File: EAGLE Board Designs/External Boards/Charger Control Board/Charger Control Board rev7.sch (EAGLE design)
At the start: 107 parts, among them K1 RELAY_DPDT, K2 RELAY_DPDT, K3 RELAY_DPDT, K4 RELAY_SOLIDSTATE_NO_, U1 VOLTAGE_REGULATOR_SOT-223_5V, U2 MCP2562FD, U3 LOGICGATE_BUFFER, U4 MCP2562FD, U7 ADM823

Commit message: Redid board layout/routing
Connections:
- net +12V: now also TP2.P$1
- net +3V3: now also TP11.P$1
- net +5V: now also TP1.P$1
- net BMS_OK: now also TP10.P$1
- net CCU_OK: now also TP8.P$1
- net GND: now also TP12.P$1
- net IMD_OK: now also TP9.P$1
- net SHDN_A: now also TP3.P$1
- net SHDN_B: now also TP4.P$1
- net SHDN_C: now also TP5.P$1
- net SHDN_D: now also TP6.P$1
- net SHDN_E: now also TP7.P$1
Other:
- moved on the sheet: TP1, TP10, TP11, TP12, TP2, TP3, TP4, TP5, TP6, TP7, TP8, TP9
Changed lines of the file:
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@@
 <attribute name="VALUE" x="134.62" y="54.61" size="1.27" layer="96" align="top-center"/>
 </instance>
-<instance part="TP6" gate="G$1" x="264.16" y="109.22" smashed="yes">
-<attribute name="NAME" x="261.62" y="110.998" size="1.27" layer="95"/>
-<attribute name="MPN" x="261.62" y="107.442" size="1.27" layer="95" align="top-left"/>
-</instance>
-<instance part="TP7" gate="G$1" x="264.16" y="101.6" smashed="yes">
-<attribute name="NAME" x="261.62" y="103.378" size="1.27" layer="95"/>
-<attribute name="MPN" x="261.62" y="99.822" size="1.27" layer="95" align="top-left"/>
-</instance>
-<instance part="TP8" gate="G$1" x="264.16" y="93.98" smashed="yes">
-<attribute name="NAME" x="261.62" y="95.758" size="1.27" layer="95"/>
-<attribute name="MPN" x="261.62" y="92.202" size="1.27" layer="95" align="top-left"/>
-</instance>
-<instance part="TP9" gate="G$1" x="264.16" y="86.36" smashed="yes">
-<attribute name="NAME" x="261.62" y="88.138" size="1.27" layer="95"/>
-<attribute name="MPN" x="261.62" y="84.582" size="1.27" layer="95" align="top-left"/>
-</instance>
-<instance part="TP10" gate="G$1" x="264.16" y="78.74" smashed="yes">
-<attribute name="NAME" x="261.62" y="80.518" size="1.27" layer="95"/>
-<attribute name="MPN" x="261.62" y="76.962" size="1.27" layer="95" align="top-left"/>
-</instance>
-<instance part="TP12" gate="G$1" x="264.16" y="71.12" smashed="yes">
-<attribute name="NAME" x="261.62" y="72.898" size="1.27" layer="95"/>
-<attribute name="MPN" x="261.62" y="69.342" size="1.27" layer="95" align="top-left"/>
-</instance>
-<instance part="TP1" gate="G$1" x="193.04" y="101.6" smashed="yes">
-<attribute name="NAME" x="190.5" y="103.378" size="1.27" layer="95"/>
-<attribute name="MPN" x="190.5" y="99.822" size="1.27" layer="95" align="top-left"/>
-</instance>
-<instance part="TP2" gate="G$1" x="193.04" y="93.98" smashed="yes">
-<attribute name="NAME" x="190.5" y="95.758" size="1.27" layer="95"/>
-<attribute name="MPN" x="190.5" y="92.202" size="1.27" layer="95" align="top-left"/>
-</instance>
-<instance part="TP3" gate="G$1" x="193.04" y="86.36" smashed="yes">
-<attribute name="NAME" x="190.5" y="88.138" size="1.27" layer="95"/>
-<attribute name="MPN" x="190.5" y="84.582" size="1.27" layer="95" align="top-left"/>
-</instance>
-<instance part="TP4" gate="G$1" x="193.04" y="78.74" smashed="yes">
-<attribute name="NAME" x="190.5" y="80.518" size="1.27" layer="95"/>
-<attribute name="MPN" x="190.5" y="76.962" size="1.27" layer="95" align="top-left"/>
-</instance>
-<instance part="TP5" gate="G$1" x="193.04" y="71.12" smashed="yes">
-<attribute name="NAME" x="190.5" y="72.898" size="1.27" layer="95"/>
-<attribute name="MPN" x="190.5" y="69.342" size="1.27" layer="95" align="top-left"/>
-</instance>
-<instance part="TP11" gate="G$1" x="193.04" y="109.22" smashed="yes">
-<attribute name="NAME" x="190.5" y="110.998" size="1.27" layer="95"/>
-<attribute name="MPN" x="190.5" y="107.442" size="1.27" layer="95" align="top-left"/>
+<instance part="TP6" gate="G$1" x="223.52" y="109.22" smashed="yes">
+<attribute name="NAME" x="220.98" y="110.998" size="1.27" layer="95"/>
+<attribute name="MPN" x="220.98" y="107.442" size="1.27" layer="95" align="top-left"/>
+</instance>
+<instance part="TP7" gate="G$1" x="223.52" y="101.6" smashed="yes">
+<attribute name="NAME" x="220.98" y="103.378" size="1.27" layer="95"/>
+<attribute name="MPN" x="220.98" y="99.822" size="1.27" layer="95" align="top-left"/>
+</instance>
+<instance part="TP8" gate="G$1" x="223.52" y="93.98" smashed="yes">
+<attribute name="NAME" x="220.98" y="95.758" size="1.27" layer="95"/>
+<attribute name="MPN" x="220.98" y="92.202" size="1.27" layer="95" align="top-left"/>
+</instance>
+<instance part="TP9" gate="G$1" x="223.52" y="86.36" smashed="yes">
+<attribute name="NAME" x="220.98" y="88.138" size="1.27" layer="95"/>
+<attribute name="MPN" x="220.98" y="84.582" size="1.27" layer="95" align="top-left"/>
+</instance>
+<instance part="TP10" gate="G$1" x="223.52" y="78.74" smashed="yes">
+<attribute name="NAME" x="220.98" y="80.518" size="1.27" layer="95"/>
+<attribute name="MPN" x="220.98" y="76.962" size="1.27" layer="95" align="top-left"/>
+</instance>
+<instance part="TP12" gate="G$1" x="223.52" y="71.12" smashed="yes">
+<attribute name="NAME" x="220.98" y="72.898" size="1.27" layer="95"/>
+<attribute name="MPN" x="220.98" y="69.342" size="1.27" layer="95" align="top-left"/>
+</instance>
+<instance part="TP1" gate="G$1" x="198.12" y="101.6" smashed="yes">
+<attribute name="NAME" x="195.58" y="103.378" size="1.27" layer="95"/>
+<attribute name="MPN" x="195.58" y="99.822" size="1.27" layer="95" align="top-left"/>
+</instance>
+<instance part="TP2" gate="G$1" x="198.12" y="93.98" smashed="yes">
+<attribute name="NAME" x="195.58" y="95.758" size="1.27" layer="95"/>
+<attribute name="MPN" x="195.58" y="92.202" size="1.27" layer="95" align="top-left"/>
+</instance>
+<instance part="TP3" gate="G$1" x="198.12" y="86.36" smashed="yes">
+<attribute name="NAME" x="195.58" y="88.138" size="1.27" layer="95"/>
+<attribute name="MPN" x="195.58" y="84.582" size="1.27" layer="95" align="top-left"/>
+</instance>
+<instance part="TP4" gate="G$1" x="198.12" y="78.74" smashed="yes">
+<attribute name="NAME" x="195.58" y="80.518" size="1.27" layer="95"/>
+<attribute name="MPN" x="195.58" y="76.962" size="1.27" layer="95" align="top-left"/>
+</instance>
+<instance part="TP5" gate="G$1" x="198.12" y="71.12" smashed="yes">
+<attribute name="NAME" x="195.58" y="72.898" size="1.27" layer="95"/>
+<attribute name="MPN" x="195.58" y="69.342" size="1.27" layer="95" align="top-left"/>
+</instance>
+<instance part="TP11" gate="G$1" x="198.12" y="109.22" smashed="yes">
+<attribute name="NAME" x="195.58" y="110.998" size="1.27" layer="95"/>
+<attribute name="MPN" x="195.58" y="107.442" size="1.27" layer="95" align="top-left"/>
 </instance>
 </instances>
@@
 <wire x1="226.06" y1="93.98" x2="228.6" y2="93.98" width="0.1524" layer="91"/>
 <label x="228.6" y="93.98" size="1.27" layer="95" xref="yes"/>
+<pinref part="TP8" gate="G$1" pin="P$1"/>
 </segment>
 </net>
@@
 <pinref part="P29" gate="1" pin="GND"/>
 <wire x1="231.14" y1="71.12" x2="231.14" y2="68.58" width="0.1524" layer="91"/>
+<pinref part="TP12" gate="G$1" pin="P$1"/>
 </segment>
 <segment>
@@
 <wire x1="200.66" y1="93.98" x2="213.36" y2="93.98" width="0.1524" layer="91"/>
 <wire x1="213.36" y1="93.98" x2="213.36" y2="96.52" width="0.1524" layer="91"/>
+<pinref part="TP2" gate="G$1" pin="P$1"/>
 </segment>
 </net>
@@
 <wire x1="226.06" y1="78.74" x2="228.6" y2="78.74" width="0.1524" layer="91"/>
 <label x="228.6" y="78.74" size="1.27" layer="95" xref="yes"/>
+<pinref part="TP10" gate="G$1" pin="P$1"/>
 </segment>
 </net>
@@
 <wire x1="226.06" y1="86.36" x2="228.6" y2="86.36" width="0.1524" layer="91"/>
 <label x="228.6" y="86.36" size="1.27" layer="95" xref="yes"/>
+<pinref part="TP9" gate="G$1" pin="P$1"/>
 </segment>
 </net>
@@
 <pinref part="P27" gate="1" pin="+5V"/>
 <wire x1="208.28" y1="104.14" x2="208.28" y2="101.6" width="0.1524" layer="91"/>
+<pinref part="TP1" gate="G$1" pin="P$1"/>
 </segment>
 </net>
@@
 <wire x1="200.66" y1="86.36" x2="203.2" y2="86.36" width="0.1524" layer="91"/>
 <label x="203.2" y="86.36" size="1.27" layer="95" xref="yes"/>
+<pinref part="TP3" gate="G$1" pin="P$1"/>
 </segment>
 </net>
@@
 <wire x1="200.66" y1="78.74" x2="203.2" y2="78.74" width="0.1524" layer="91"/>
 <label x="203.2" y="78.74" size="1.27" layer="95" xref="yes"/>
+<pinref part="TP4" gate="G$1" pin="P$1"/>
 </segment>
 </net>
@@
 <wire x1="200.66" y1="71.12" x2="203.2" y2="71.12" width="0.1524" layer="91"/>
 <label x="203.2" y="71.12" size="1.27" layer="95" xref="yes"/>
+<pinref part="TP5" gate="G$1" pin="P$1"/>
 </segment>
 </net>
@@
 <wire x1="226.06" y1="101.6" x2="228.6" y2="101.6" width="0.1524" layer="91"/>
 <label x="228.6" y="101.6" size="1.27" layer="95" xref="yes"/>
+<pinref part="TP7" gate="G$1" pin="P$1"/>
 </segment>
 </net>
@@
 <wire x1="226.06" y1="109.22" x2="228.6" y2="109.22" width="0.1524" layer="91"/>
 <label x="228.6" y="109.22" size="1.27" layer="95" xref="yes"/>
+<pinref part="TP6" gate="G$1" pin="P$1"/>
 </segment>
 </net>
@@
 <pinref part="P51" gate="G$1" pin="+3V3"/>
 <wire x1="203.2" y1="111.76" x2="203.2" y2="109.22" width="0.1524" layer="91"/>
-</segment>
-</net>
+<pinref part="TP11" gate="G$1" pin="P$1"/>
+</segment>
+</net>

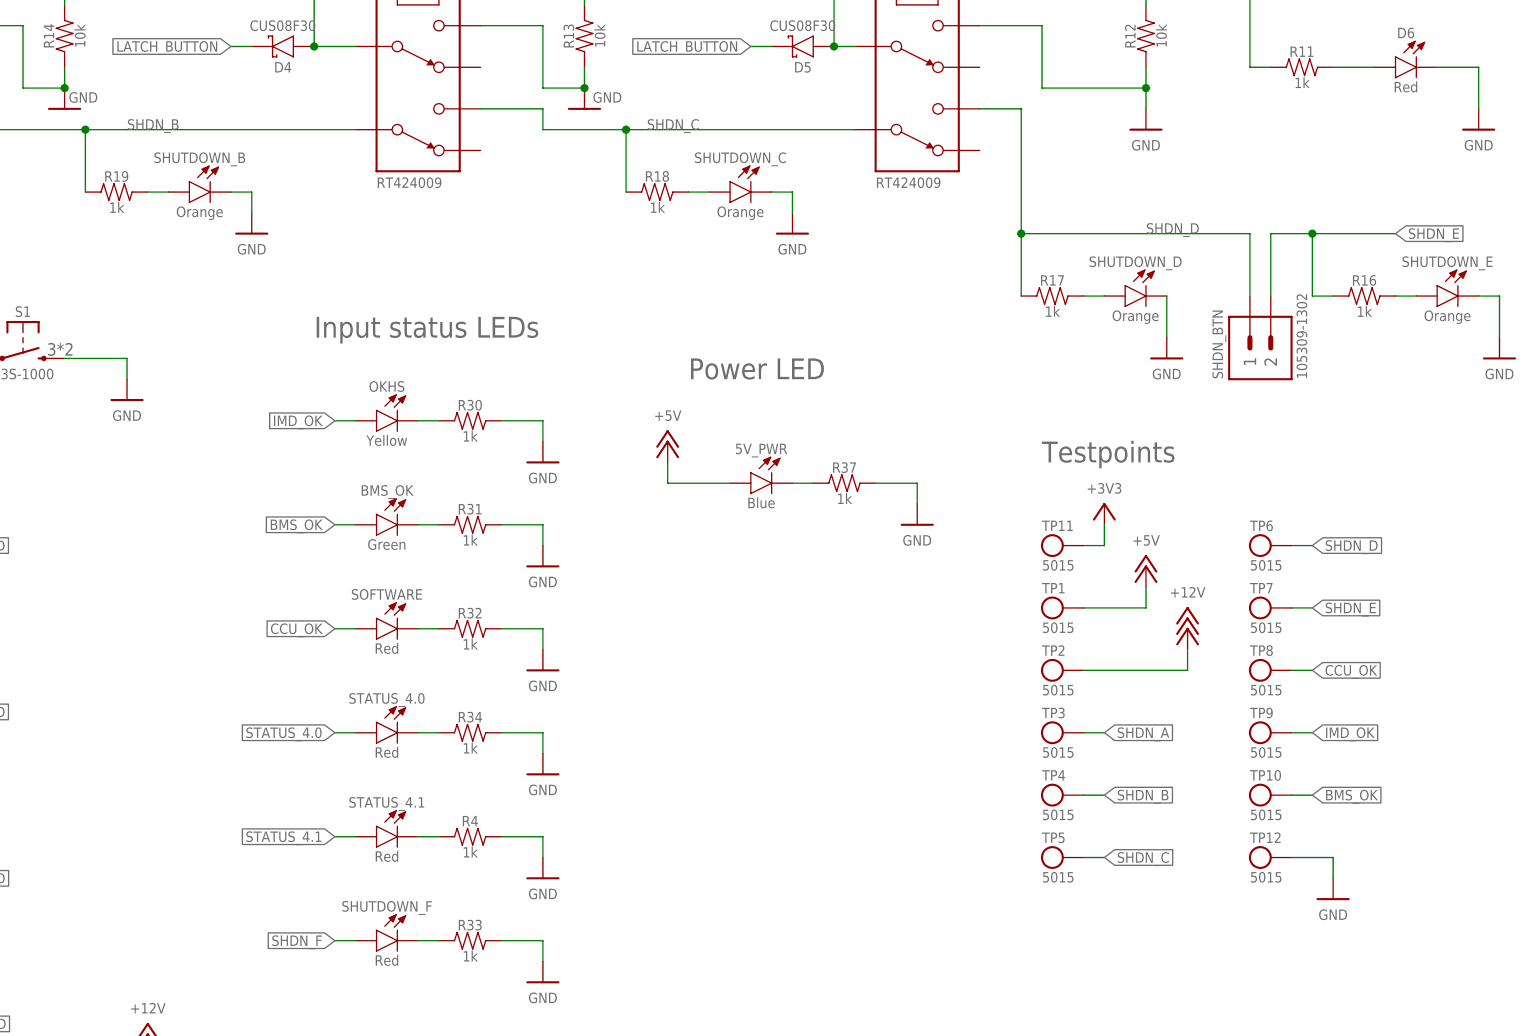
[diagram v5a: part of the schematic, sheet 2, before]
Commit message: Rearranged layout, cleaned up silkscreen
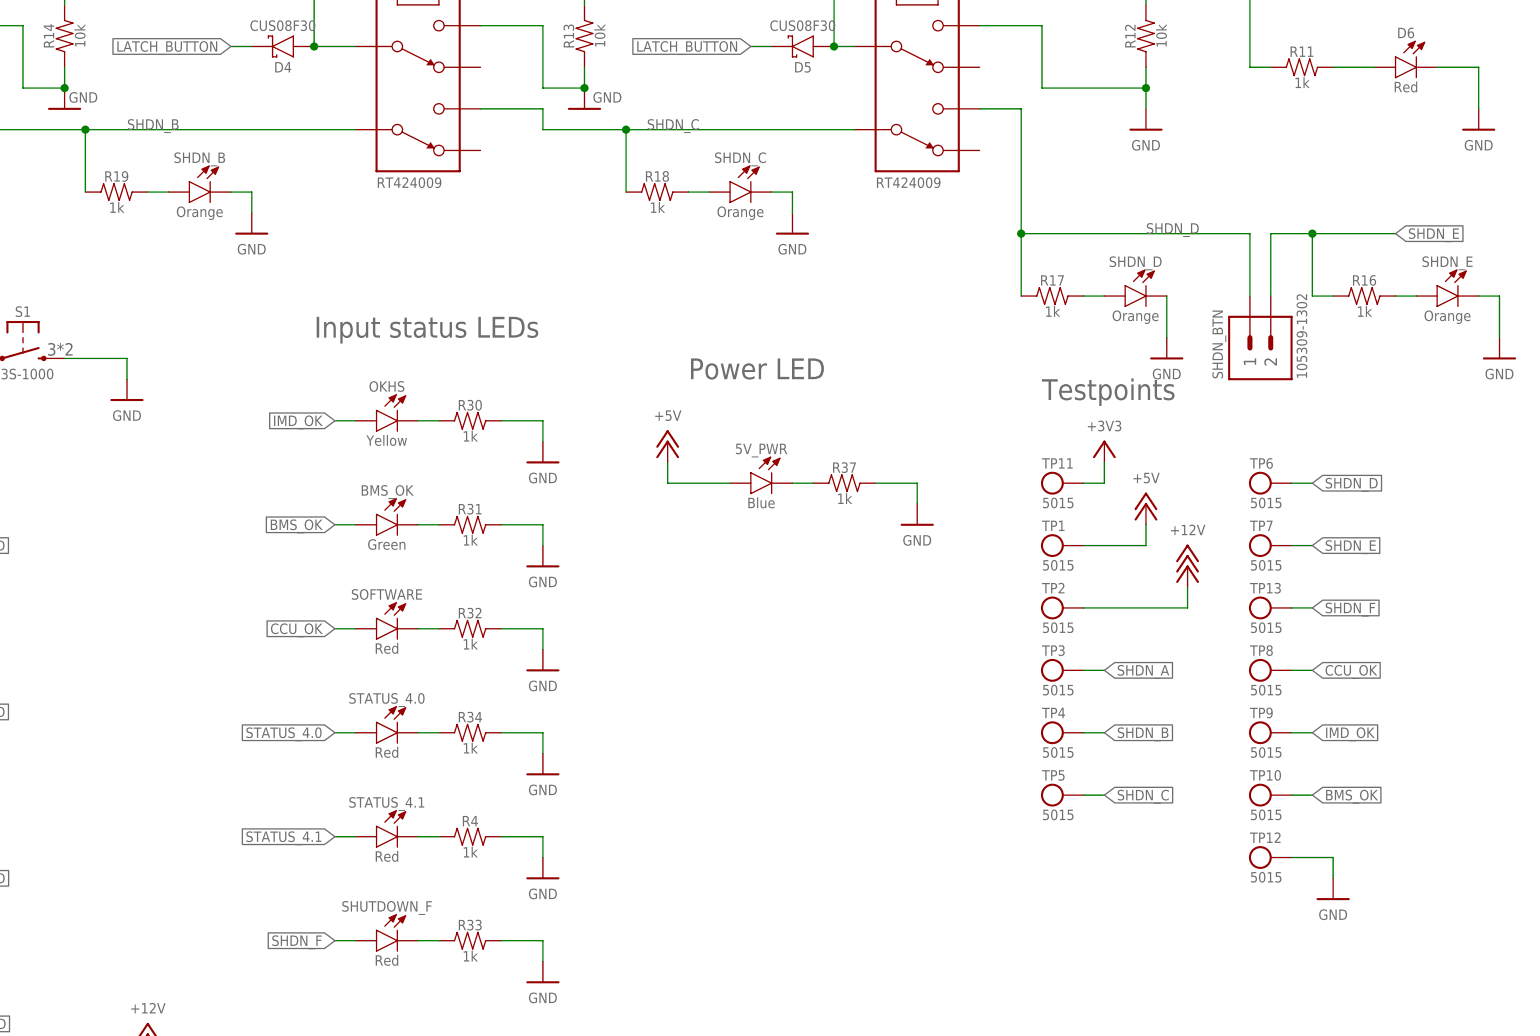
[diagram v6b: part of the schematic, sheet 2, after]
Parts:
- added TP13: TEST_POINT, HyTechDevices:TEST_POINT
- renumbered SHUTDOWN_B to SHDN_B, SHUTDOWN_C to SHDN_C, SHUTDOWN_D to SHDN_D, SHUTDOWN_E to SHDN_E
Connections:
- net SHDN_F: now also TP13.P$1
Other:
- moved on the sheet: TP1, TP11, TP2, TP3, TP4, TP5, TP6, TP7

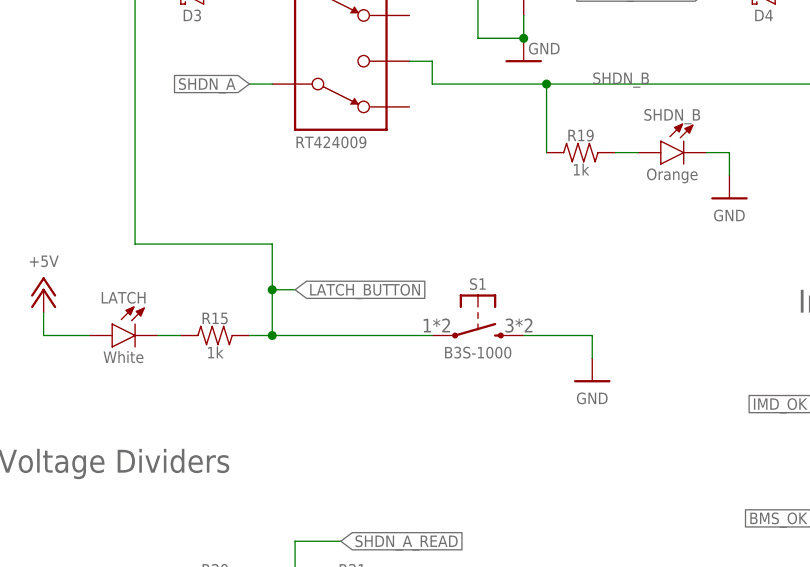
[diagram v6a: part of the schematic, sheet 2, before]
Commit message: Cleaned up silkscreen, added logo and description
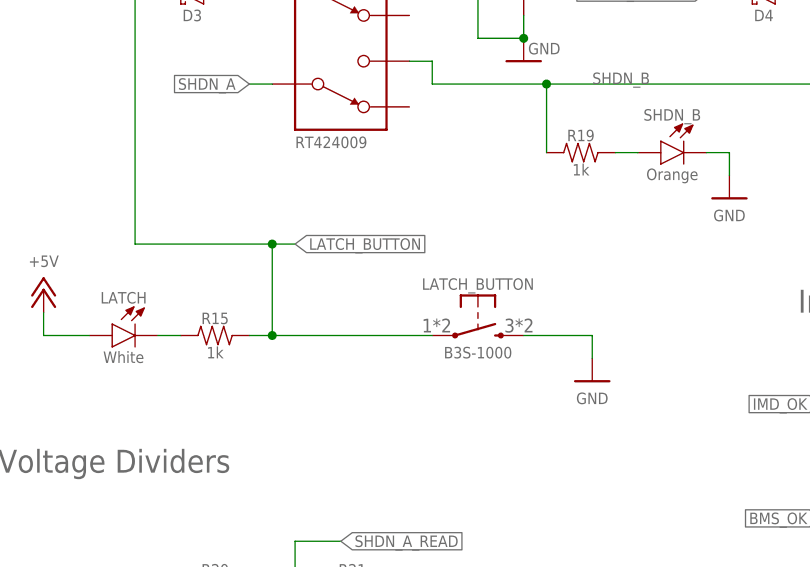
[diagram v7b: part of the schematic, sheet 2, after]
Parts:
- renumbered S1 to LATCH_BUTTON
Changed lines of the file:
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@@
 <part name="U2" library="HyTechDevices" deviceset="MCP2562FD" device=""/>
 <part name="P17" library="HyTechSupplies" deviceset="GND" device=""/>
-<part name="S1" library="HyTechDevices" deviceset="BUTTON" device=""/>
+<part name="LATCH_BUTTON" library="HyTechDevices" deviceset="BUTTON" device=""/>
 <part name="P59" library="HyTechSupplies" deviceset="+3V3" device=""/>
 <part name="U3" library="HyTechDevices" deviceset="LOGICGATE_BUFFER" device=""/>
@@
 <attribute name="MPN" x="166.37" y="172.085" size="1.27" layer="96" rot="R180" align="top-center"/>
 </instance>
-<instance part="S1" gate="G$1" x="68.58" y="132.08" smashed="yes">
+<instance part="LATCH_BUTTON" gate="G$1" x="68.58" y="132.08" smashed="yes">
 <attribute name="NAME" x="71.12" y="137.16" size="1.27" layer="95" align="bottom-center"/>
 <attribute name="MPN" x="71.12" y="130.81" size="1.27" layer="96" align="top-center"/>
@@
 <wire x1="76.2" y1="132.08" x2="83.82" y2="132.08" width="0.1524" layer="91"/>
 <wire x1="83.82" y1="132.08" x2="83.82" y2="129.54" width="0.1524" layer="91"/>
-<pinref part="S1" gate="G$1" pin="S"/>
+<pinref part="LATCH_BUTTON" gate="G$1" pin="S"/>
 </segment>
 <segment>
@@
 <pinref part="R15" gate="G$1" pin="2"/>
 <wire x1="48.26" y1="132.08" x2="45.72" y2="132.08" width="0.1524" layer="91"/>
-<wire x1="48.26" y1="132.08" x2="48.26" y2="137.16" width="0.1524" layer="91"/>
+<wire x1="48.26" y1="132.08" x2="48.26" y2="142.24" width="0.1524" layer="91"/>
 <junction x="48.26" y="132.08"/>
-<wire x1="48.26" y1="137.16" x2="50.8" y2="137.16" width="0.1524" layer="91"/>
-<label x="50.8" y="137.16" size="1.27" layer="95" xref="yes"/>
+<wire x1="48.26" y1="142.24" x2="50.8" y2="142.24" width="0.1524" layer="91"/>
+<label x="50.8" y="142.24" size="1.27" layer="95" xref="yes"/>
 <wire x1="33.02" y1="170.18" x2="35.56" y2="170.18" width="0.1524" layer="91"/>
 <wire x1="33.02" y1="170.18" x2="33.02" y2="142.24" width="0.1524" layer="91"/>
 <wire x1="33.02" y1="142.24" x2="48.26" y2="142.24" width="0.1524" layer="91"/>
-<wire x1="48.26" y1="142.24" x2="48.26" y2="137.16" width="0.1524" layer="91"/>
-<junction x="48.26" y="137.16"/>
+<junction x="48.26" y="142.24"/>
 <pinref part="D3" gate="G$1" pin="C"/>
-<pinref part="S1" gate="G$1" pin="P"/>
-</segment>
-<segment>
+<pinref part="LATCH_BUTTON" gate="G$1" pin="P"/>
+</segment>
+<segment>
